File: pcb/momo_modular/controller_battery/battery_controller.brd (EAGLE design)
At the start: 31.7 x 33 mm, 33 parts, among them U1 XRP7659, U2 MAX1555, U3 MCP1702, U4 PIC24F16KA101-X_PSSOP, U5 FLASH8MSOP8

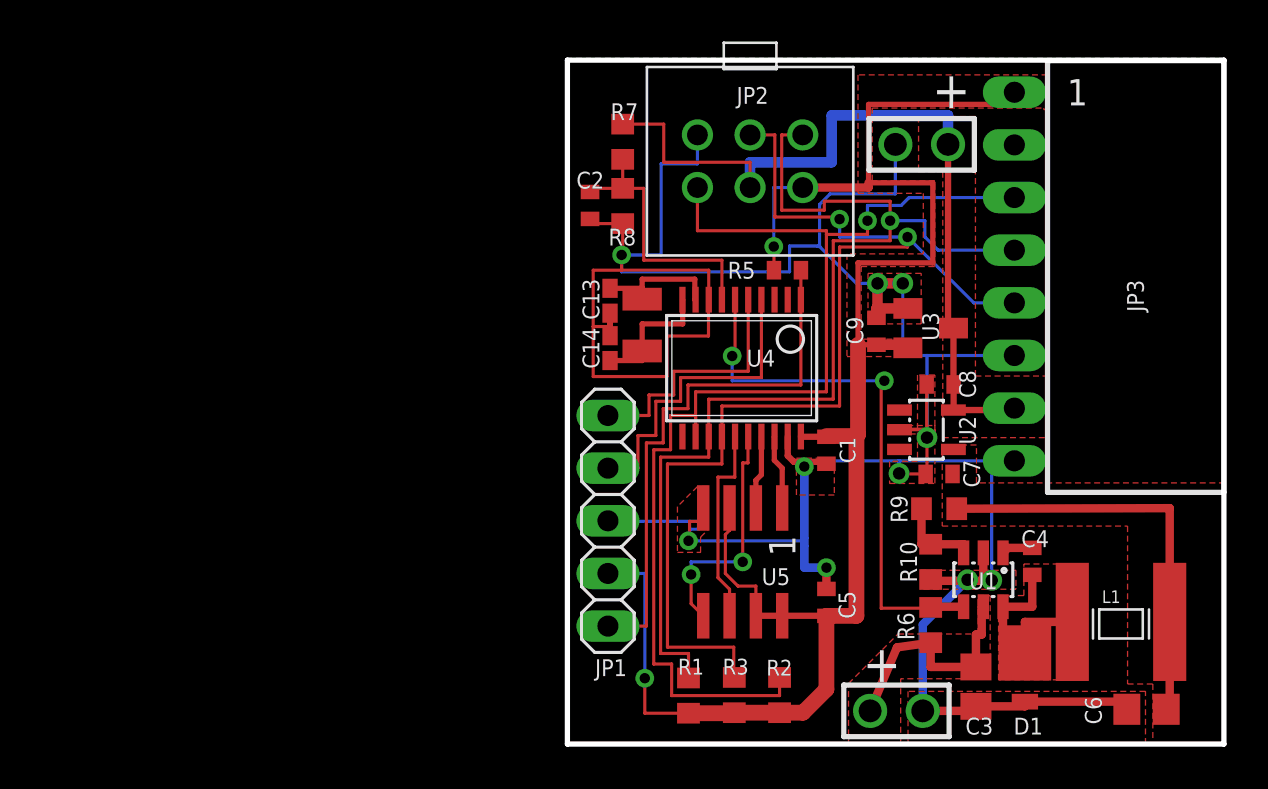
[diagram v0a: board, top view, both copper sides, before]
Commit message: Begin work on resource manager and revised task manager on pic24.  Started relaying out controller board and combining functionality.
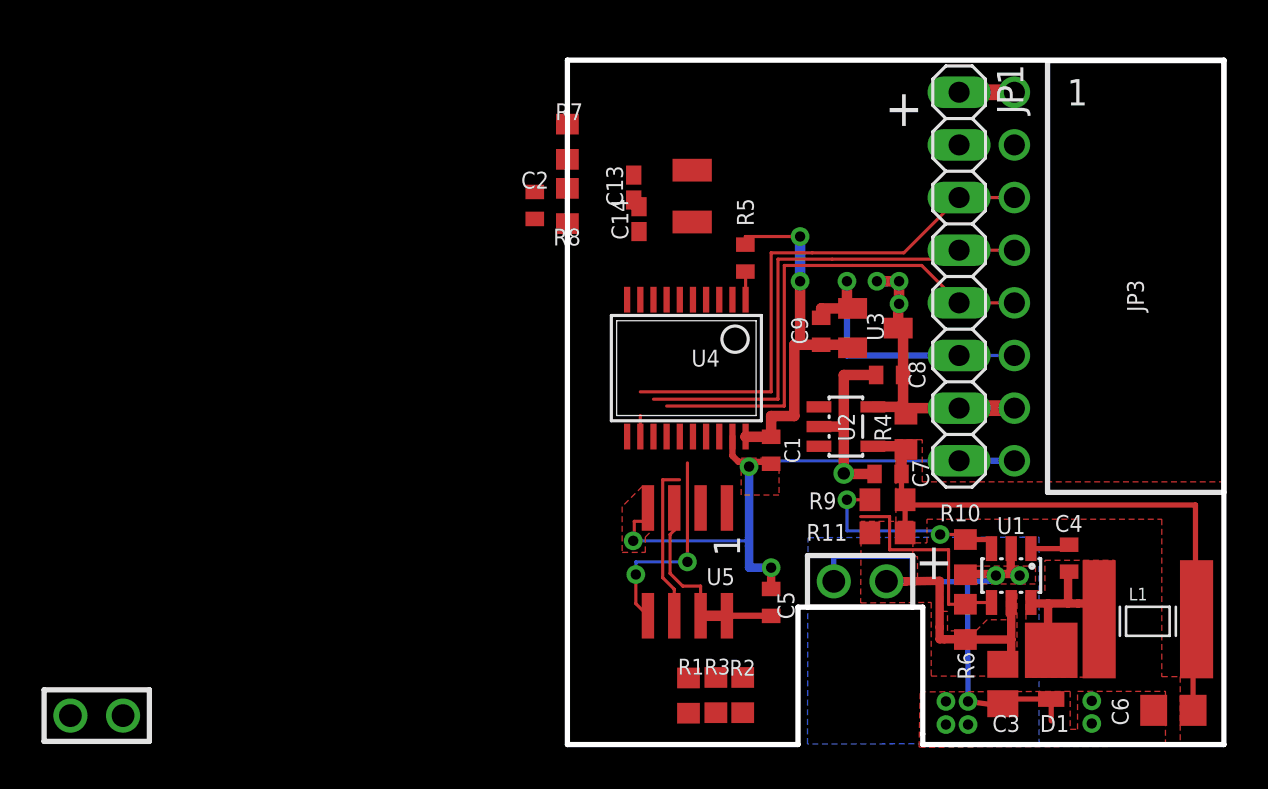
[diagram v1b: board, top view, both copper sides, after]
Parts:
- removed JP2: MOMO-SENSOR-HEADER, components:2X3-MOLEX-90130
- removed JP4, JP5: MOMO-EDGE-POWER-M, components:MOMO-EDGE-SMALL-2M
- added R11, R4: 0R, rcl:R0603
- added U$1, U$2: MOMO-EDGE-POWER-M, components:MOMO-EDGE-SMALL-2M
- JP1: value (none) -> MOMO-VERT-8M; device pinhead:1X05 -> components:1X08
- moved JP1 20.6 mm to (53.1, 34.6), turned to 270 degrees
- moved XTAL1 6.67 mm to (40.3, 39.8)
- moved C14 6.38 mm to (37.7, 37.4)
- moved C13 5.58 mm to (37.4, 38.9)
- moved U2 3.89 mm to (47.7, 27.4)
- moved C2 2.67 mm to (32.7, 38.1)
- moved C9 2.67 mm to (46.5, 32.0)
- moved R7 2.67 mm to (34.2, 41.1)
- moved R8 2.67 mm to (34.2, 38.0)
- moved U3 2.67 mm to (49.1, 32.2)
- moved U4 2.67 mm to (40.0, 30.2)
- moved U5 2.67 mm to (40.0, 20.9)
- moved C1 2.67 mm to (44.1, 26.3)
- moved C5 2.67 mm to (44.1, 18.9)
- moved R9 2.53 mm to (49.7, 23.9)
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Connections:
- removed net N$1: JP1.4, U4.4
- removed net N$2: JP1.5, U4.5
- net +18V: now also R11.1, U$1.2; no longer JP5.1
- net GND: now also JP1.6, JP1.8, U$1.1, U$2.1; no longer JP1.3, JP2.6, JP4.2, JP5.2
- net ICLK: now also JP1.3; no longer JP2.3
- net IDAT: now also JP1.4; no longer JP2.4
- net IRQ: now also JP1.5; no longer JP2.5
- net N$15: no longer JP1.1
- net N$5: now also R11.2, R4.1
- net V+: now also JP1.7, R4.2, U$2.2; no longer JP2.2, JP4.1
- net VCCINT: now also JP1.1; no longer JP1.2, JP2.1
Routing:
- net GND: track 150.6 -> 83.9 mm, vias 10 -> 13
- net VCCINT: track 85.7 -> 30.5 mm
- net ICLK: track 58.7 -> 26.9 mm, vias 1 -> 0
- net IRQ: track 55.0 -> 24.3 mm, vias 2 -> 0
- net IDAT: track 52.8 -> 24.3 mm, vias 1 -> 0
- net N$15: track 26.5 -> 1.50 mm
- net V+: track 39.8 -> 15.9 mm, vias 0 -> 3
- net N$9: track 26.5 -> 10.6 mm, vias 2 -> 0
- net N$1: track 15.5 -> 0.00 mm
- net N$6: track 13.3 -> 0.17 mm
- net N$2: track 12.4 -> 0.00 mm
- net N$5: track 20.0 -> 30.2 mm
- net N$25: track 6.61 -> 0.00 mm
- net N$24: track 6.46 -> 0.00 mm
- net N$10: track 4.16 -> 10.5 mm, vias 0 -> 2
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- removed copper zone on layer 1, net V+
- removed copper zone on layer 1, net VCCINT
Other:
- outline, holes or cut-outs redrawn
